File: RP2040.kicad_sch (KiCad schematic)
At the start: 27 parts, among them J1 USB_B_Micro, J2 Conn_01x02, U1 AMS1117-3.3, U5 W25Q128JVS, U6 RP2040, Y1 X322512MSB4SI

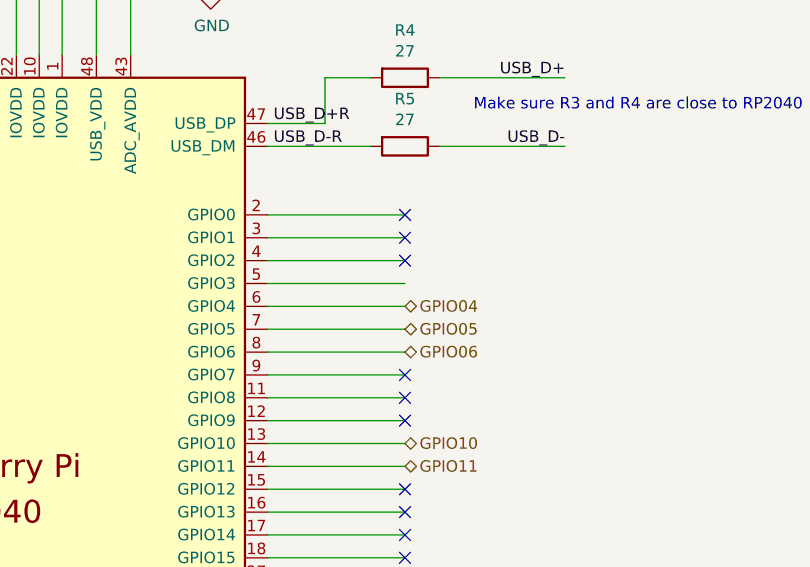
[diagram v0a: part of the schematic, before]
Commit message: Passes design rule checks
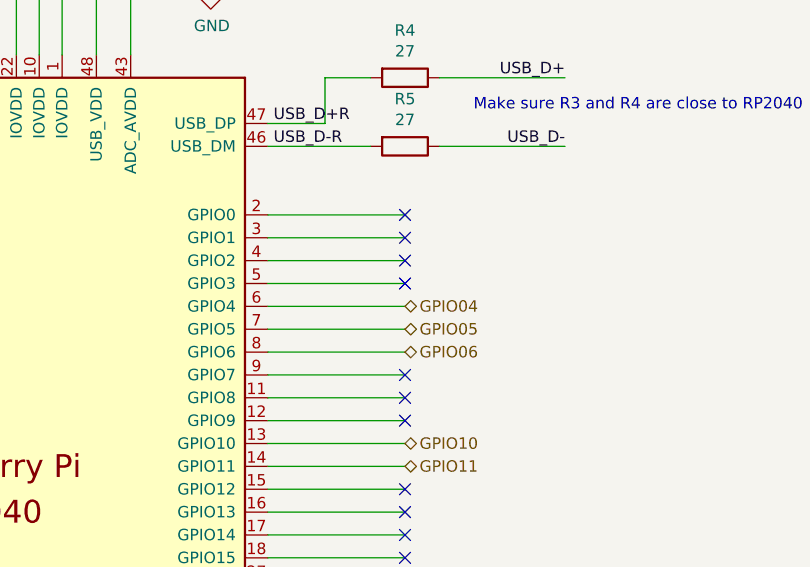
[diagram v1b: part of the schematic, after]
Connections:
- no-connect marks 25 -> 26
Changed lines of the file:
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@@
   (no_connect (at 227.33 123.19))
   (no_connect (at 227.33 105.41))
+  (no_connect (at 227.33 80.01))
   (no_connect (at 227.33 92.71))
   (no_connect (at 227.33 102.87))

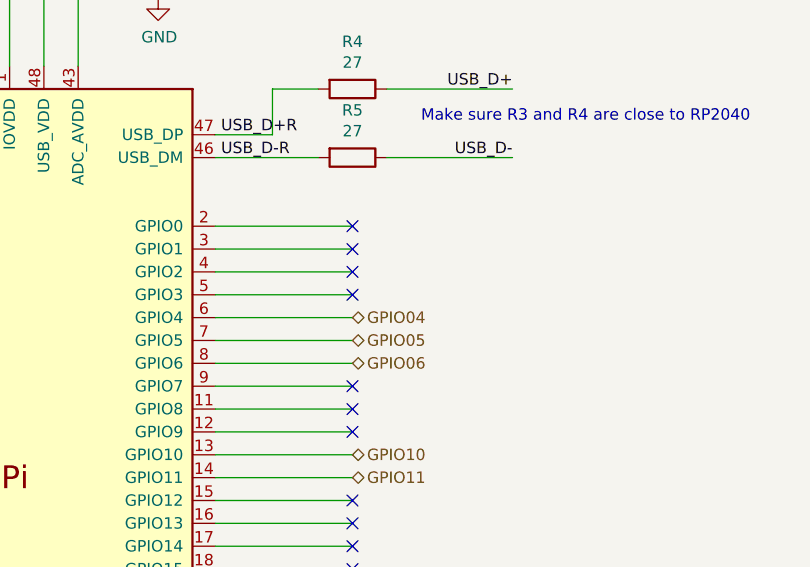
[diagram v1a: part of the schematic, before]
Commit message: Correct pin assignment for I2C, add via stitching
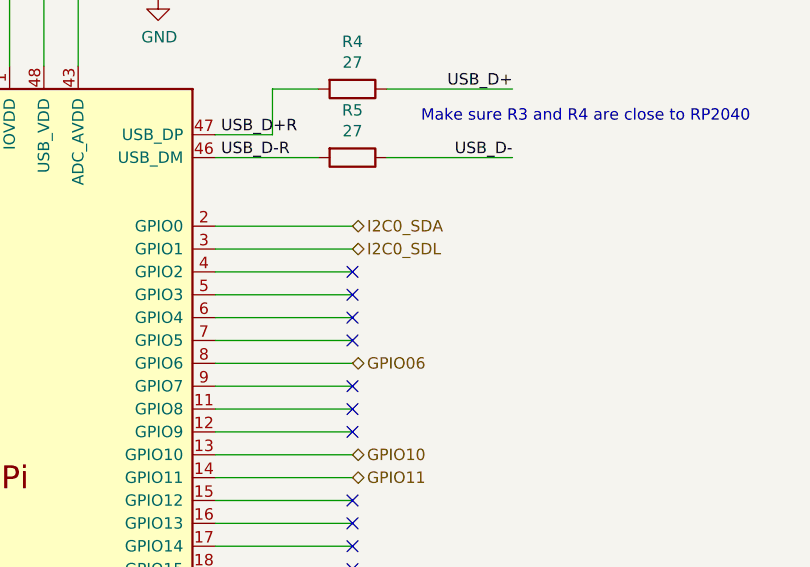
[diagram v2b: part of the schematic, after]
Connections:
- net I2C0_SDA: now reaches U6.2 (GPIO0)
- net I2C0_SDL: now reaches U6.3 (GPIO1)
- net GPIO04: no longer names the net of U6.6 (GPIO4)
- net GPIO05: no longer names the net of U6.7 (GPIO5)
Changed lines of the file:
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@@
   (no_connect (at 227.33 90.17))
   (no_connect (at 227.33 95.25))
-  (no_connect (at 227.33 72.39))
   (no_connect (at 227.33 135.89))
   (no_connect (at 227.33 128.27))
   (no_connect (at 227.33 118.11))
-  (no_connect (at 227.33 74.93))
   (no_connect (at 227.33 77.47))
   (no_connect (at 227.33 140.97))
@@
   (no_connect (at 227.33 80.01))
   (no_connect (at 227.33 92.71))
+  (no_connect (at 227.33 82.55))
+  (no_connect (at 227.33 85.09))
   (no_connect (at 227.33 102.87))
   (no_connect (at 227.33 125.73))
@@
     (effects (font (size 1.27 1.27)) (justify left))
   )
-  (hierarchical_label "GPIO05" (shape bidirectional) (at 227.33 85.09 0)
+  (hierarchical_label "I2C0_SDL" (shape bidirectional) (at 227.33 74.93 0)
+    (effects (font (size 1.27 1.27)) (justify left))
+  )
+  (hierarchical_label "I2C0_SDA" (shape bidirectional) (at 227.33 72.39 0)
     (effects (font (size 1.27 1.27)) (justify left))
   )
@@
     (effects (font (size 1.27 1.27)) (justify left))
   )
-  (hierarchical_label "GPIO04" (shape bidirectional) (at 227.33 82.55 0)
-    (effects (font (size 1.27 1.27)) (justify left))
-  )

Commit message: JLCPCB rotation cleanup, kibot script fixes
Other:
- title: CJ4 Autopilot Panel -> Collins FMS 3000
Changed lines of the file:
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@@
   (paper "A4")
   (title_block
-    (title "CJ4 Autopilot Panel")
-    (date "2022-08-30")
-    (rev "@version@")
+    (title "Collins FMS 3000")
+    (date "2022-11-02")
+    (rev "")
     (comment 1 "neile@live.com")
     (comment 2 "Neil Enns")

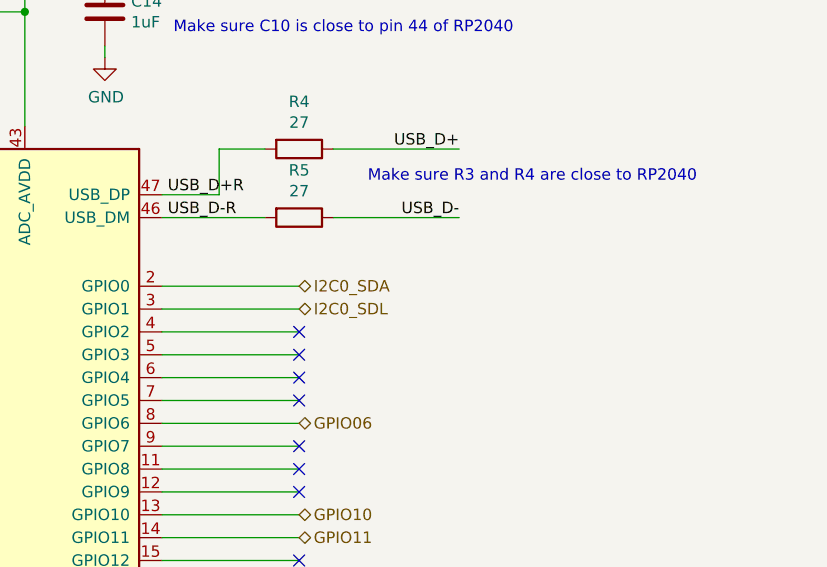
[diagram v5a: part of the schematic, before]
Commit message: Lots of pre-work before replacing RP2040 layout
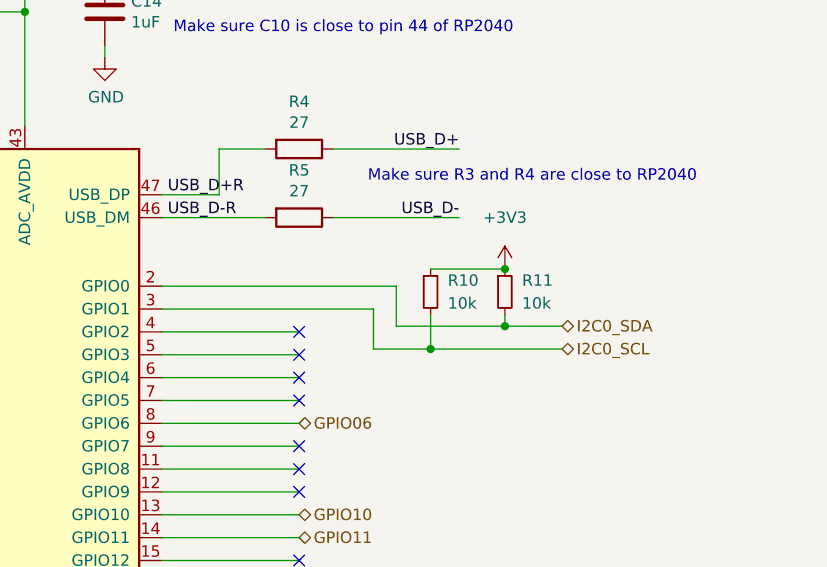
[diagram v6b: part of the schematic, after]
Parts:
- added R10, R11: 10k, Resistor_SMD:R_1206_3216Metric_Pad1.30x1.75mm_HandSolder, symbol Device:R_Small
- C10, C11, C13, C15, C16, C17, C18, C19, C20, C8: footprint Collins-FMS-3000:Perfect_0402 -> Custom_Footprints:Perfect_0402; LCSC C1525 -> (none); MPN - JLCPCB (none) -> C1525
- C12, C14: footprint Collins-FMS-3000:Perfect_0402 -> Custom_Footprints:Perfect_0402; LCSC C52923 -> (none); MPN - JLCPCB (none) -> C52923
- C5, C6: footprint Collins-FMS-3000:Perfect_0402 -> Custom_Footprints:Perfect_0402; LCSC C32949 -> (none); MPN - JLCPCB (none) -> C32949
- C7, C9: LCSC C19702 -> (none); MPN - JLCPCB (none) -> C19702
- R1, R2: footprint Collins-FMS-3000:Perfect_0402 -> Custom_Footprints:Perfect_0402; LCSC C11702 -> (none); MPN - JLCPCB (none) -> C11702
- R4, R5: LCSC C25190 -> (none); MPN - JLCPCB (none) -> C25190
- U1: LCSC C6186 -> (none); MPN - JLCPCB (none) -> C6186
- U5: LCSC C97521 -> (none); MPN - JLCPCB (none) -> C97521
- U6: LCSC C2040 -> (none); MPN - JLCPCB (none) -> C2040
- Y1: LCSC C9002 -> (none); MPN - JLCPCB (none) -> C9002
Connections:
- net +3V3: now also R10.1, R11.1
- net I2C0_SDA: now also R11.2
- net I2C0_SDL renamed I2C0_SCL
- net I2C0_SCL: now also R10.2

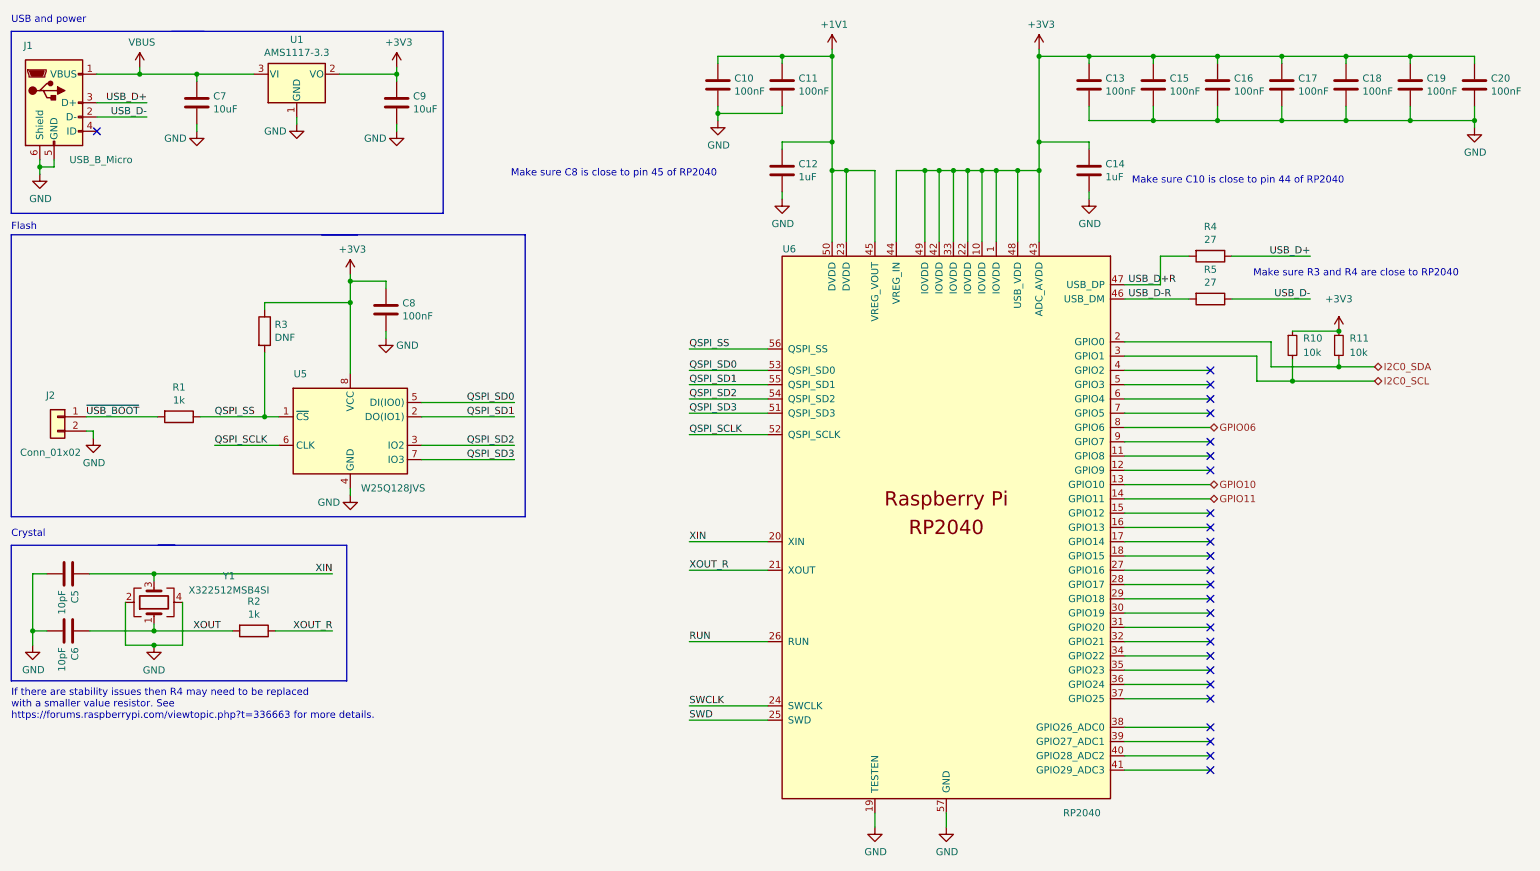
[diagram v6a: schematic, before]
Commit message: New RP2040 layout added
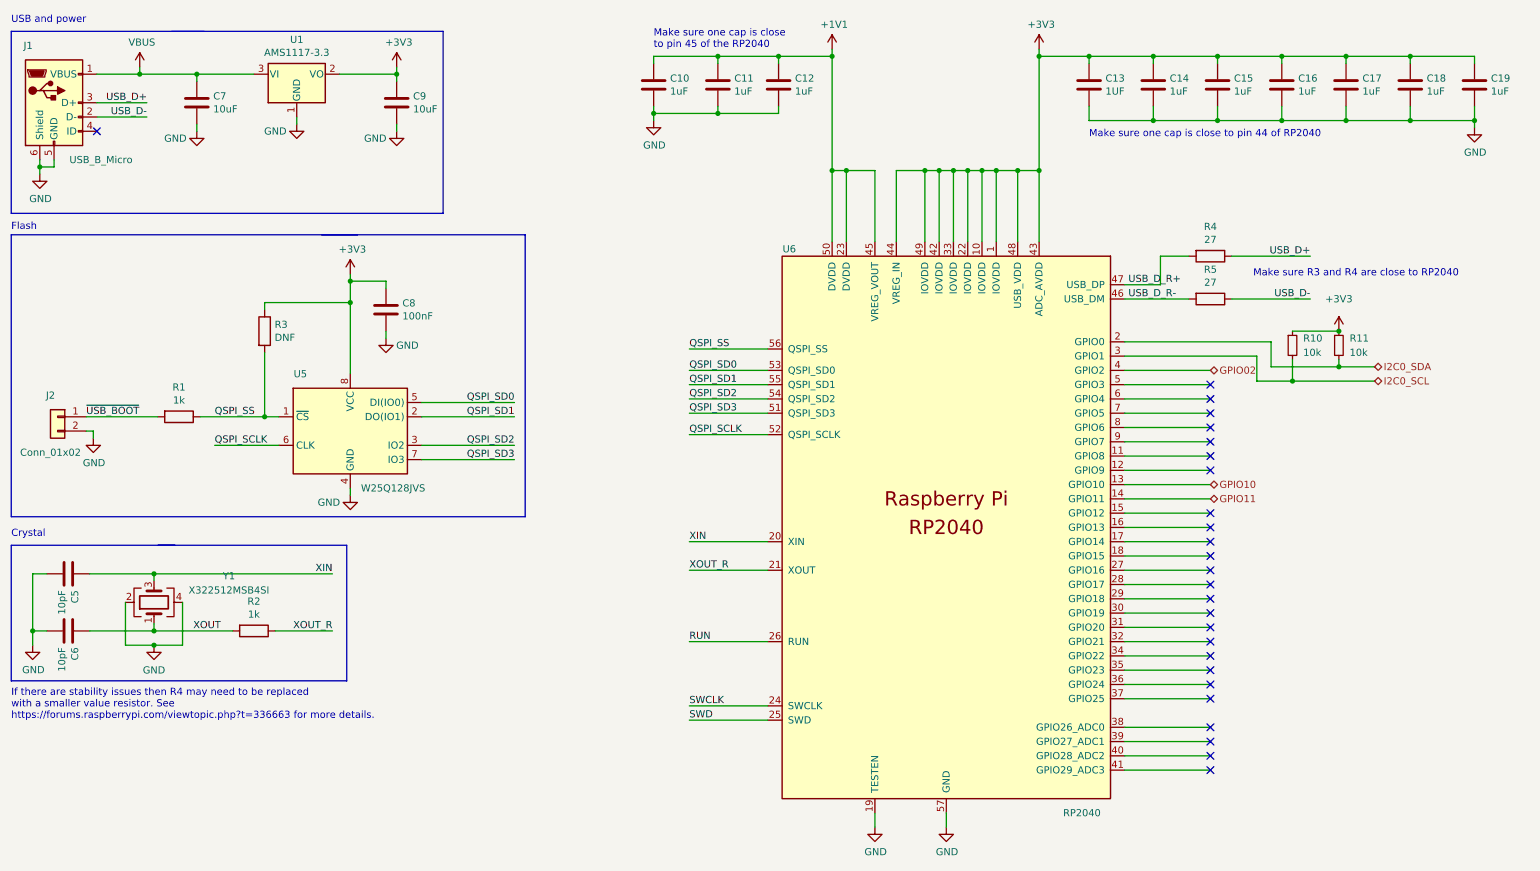
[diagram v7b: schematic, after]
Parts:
- removed C14: 1uF, Custom_Footprints:Perfect_0402, symbol Device:C
- C10, C11: value 100nF -> 1uF
- C13: value 100nF -> 1UF
- C14: renamed from C15; value 100nF -> 1uF
- C15: renamed from C16; value 100nF -> 1uF
- C16: renamed from C17; value 100nF -> 1uF
- C17: renamed from C18; value 100nF -> 1uF
- C18: renamed from C19; value 100nF -> 1uF
- C19: renamed from C20; value 100nF -> 1uF
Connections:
- net GPIO02: now reaches U6.4 (GPIO2)
- net GPIO06: no longer names the net of U6.8 (GPIO6)
- net USB_D+R renamed USB_D_R+
- net USB_D-R renamed USB_D_R-
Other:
- note added: "Make sure one cap is close to pin 44 of RP2040"
- note added: "Make sure one cap is close to pin 45 of the RP2040"
- note removed: "Make sure C10 is close to pin 44 of RP2040"
- note removed: "Make sure C8 is close to pin 45 of RP2040"
- moved on the sheet: C10, C11, C12

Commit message: FULLY ROUTED
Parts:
- C10, C11, C14, C15, C16, C17, C18, C19: MPN - JLCPCB C1525 -> C52923
- U6: footprint RP2040_minimal:RP2040-QFN-56 -> Custom_Footprints:QFN56P40_700X700X90L40X18T310N
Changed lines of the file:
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@@
       (effects (font (size 1.27 1.27)) hide)
     )
-    (property "MPN - JLCPCB" "C1525" (id 6) (at 274.32 26.67 0)
+    (property "MPN - JLCPCB" "C52923" (id 6) (at 274.32 26.67 0)
       (effects (font (size 1.27 1.27)) hide)
     )
@@
       (effects (font (size 1.27 1.27)) hide)
     )
-    (property "MPN - JLCPCB" "C1525" (id 6) (at 217.17 26.67 0)
+    (property "MPN - JLCPCB" "C52923" (id 6) (at 217.17 26.67 0)
       (effects (font (size 1.27 1.27)) hide)
     )
@@
       (effects (font (size 1.27 1.27)) hide)
     )
-    (property "MPN - JLCPCB" "C1525" (id 6) (at 139.7 26.67 0)
+    (property "MPN - JLCPCB" "C52923" (id 6) (at 139.7 26.67 0)
       (effects (font (size 1.27 1.27)) hide)
     )
@@
     (property "Reference" "U6" (id 0) (at 152.4 55.88 0))
     (property "Value" "RP2040" (id 1) (at 204.47 156.21 0))
-    (property "Footprint" "RP2040_minimal:RP2040-QFN-56" (id 2) (at 161.29 105.41 0)
+    (property "Footprint" "Custom_Footprints:QFN56P40_700X700X90L40X18T310N" (id 2) (at 161.29 105.41 0)
       (effects (font (size 1.27 1.27)) hide)
     )
@@
       (effects (font (size 1.27 1.27)) hide)
     )
-    (property "MPN - JLCPCB" "C1525" (id 6) (at 128.27 26.67 0)
+    (property "MPN - JLCPCB" "C52923" (id 6) (at 128.27 26.67 0)
       (effects (font (size 1.27 1.27)) hide)
     )
@@
       (effects (font (size 1.27 1.27)) hide)
     )
-    (property "MPN - JLCPCB" "C1525" (id 6) (at 251.46 26.67 0)
+    (property "MPN - JLCPCB" "C52923" (id 6) (at 251.46 26.67 0)
       (effects (font (size 1.27 1.27)) hide)
     )
@@
       (effects (font (size 1.27 1.27)) hide)
     )
-    (property "MPN - JLCPCB" "C1525" (id 6) (at 228.6 26.67 0)
+    (property "MPN - JLCPCB" "C52923" (id 6) (at 228.6 26.67 0)
       (effects (font (size 1.27 1.27)) hide)
     )
@@
       (effects (font (size 1.27 1.27)) hide)
     )
-    (property "MPN - JLCPCB" "C1525" (id 6) (at 240.03 26.67 0)
+    (property "MPN - JLCPCB" "C52923" (id 6) (at 240.03 26.67 0)
       (effects (font (size 1.27 1.27)) hide)
     )
@@
       (effects (font (size 1.27 1.27)) hide)
     )
-    (property "MPN - JLCPCB" "C1525" (id 6) (at 262.89 26.67 0)
-      (effects (font (size 1.27 1.27)) hide)
-    )
+    (property "MPN - JLCPCB" "C52923" (id 6) (at 262.89 26.67 0)
+      (effects (font (size 1.27 1.27)) hide)
+    )
